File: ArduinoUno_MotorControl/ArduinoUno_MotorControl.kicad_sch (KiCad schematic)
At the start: 10 parts, among them J1 Power, J2 Analog, J3 Digital, J4 Digital, J5 Conn_01x08, J6 Conn_01x06, J7 Conn_01x02, M1 Motor_DC, M2 Motor_DC

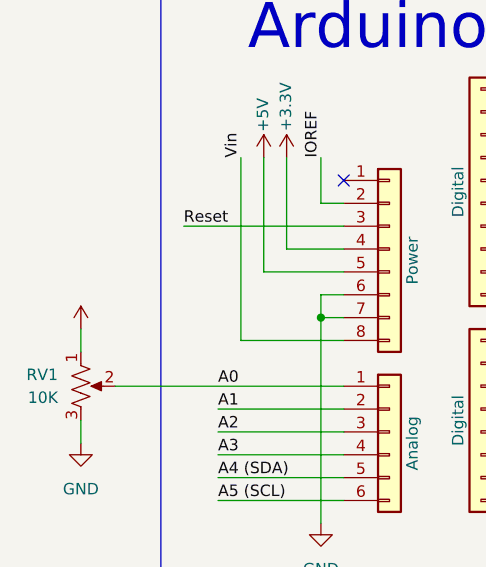
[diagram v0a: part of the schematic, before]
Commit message: Fixed spelling error.
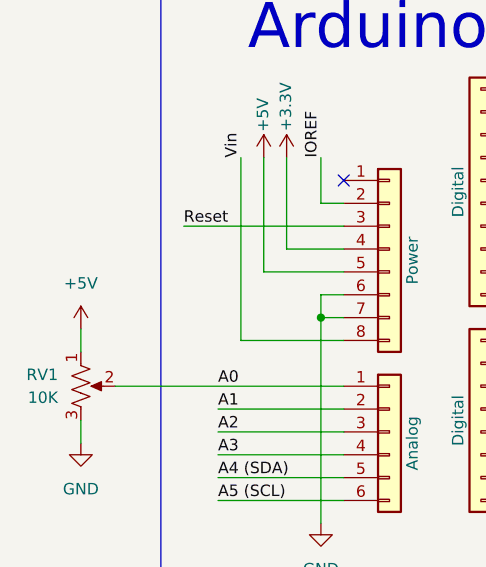
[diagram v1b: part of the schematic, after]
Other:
- title: Aruino Uno With DC Motor Controller -> Arduino Uno With DC Motor Controller
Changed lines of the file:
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@@
   (paper "A4")
   (title_block
-    (title "Aruino Uno With DC Motor Controller")
-    (date "2022-03-28")
-    (rev "0.1")
+    (title "Arduino Uno With DC Motor Controller")
+    (date "2022-07-13")
+    (rev "0.2")
     (company "Woolsey Workshop")
     (comment 1 "By John Woolsey")
@@
       (effects (font (size 1.27 1.27)) hide)
     )
-    (property "Value" "" (id 1) (at 52.07 72.39 0))
+    (property "Value" "+5V" (id 1) (at 52.07 72.39 0))
     (property "Footprint" "" (id 2) (at 52.07 77.47 0)
       (effects (font (size 1.27 1.27)) hide)
